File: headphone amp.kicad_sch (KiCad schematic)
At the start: 48 parts, among them J1 USB_B_Micro, J2 AudioJack2_Ground_Switch, J3 AudioJack2_Ground_Switch, U1 MAX660CPA+, U2 MAX660CPA+, U3 NE5532, U4 NE5532, U5 NE5532, U6 NE5532

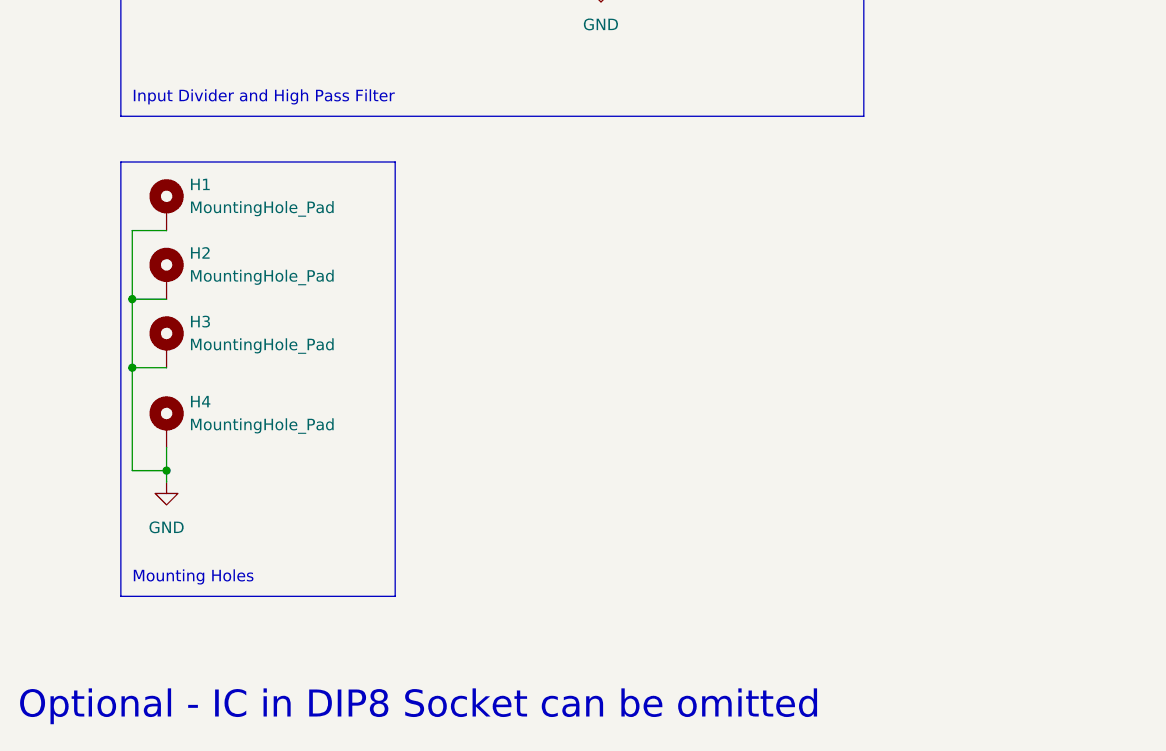
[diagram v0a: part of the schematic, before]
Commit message: Rounded Corners, Signature and Updated Fab files
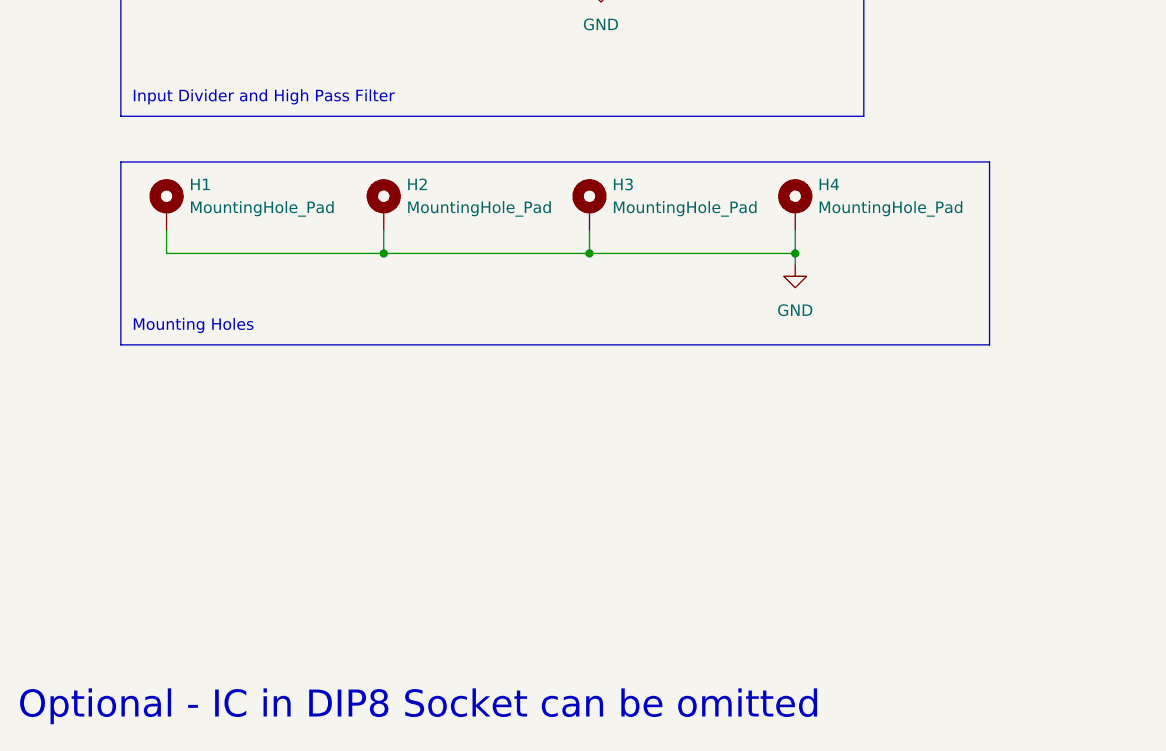
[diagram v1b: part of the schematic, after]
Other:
- moved on the sheet: H2, H3, H4
